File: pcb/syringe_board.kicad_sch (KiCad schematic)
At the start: 33 parts, among them J1 PJ-037A, J2 0855025008, J3 OSTVN08A150, J4 10118194-0001LF, J5 PPTC161LFBN-RC, J6 PPTC121LFBN-RC, U1 TMC2208, U2 ROF-78E3.3-0.5SMD-R, U3 ATMEGA32U4, X1 feather_wing, Y1 8MHz

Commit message: pcb updates in progress
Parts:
- removed J1: PJ-037A, asl_footprints:DC_Jack, symbol asl_symbols:PJ-037A
- removed J4: 10118194-0001LF, asl_footprints:microUSB_horizontal_socket, symbol asl_symbols:USB_micro_horz_socket_reinforced
- removed JP1, JP2: SolderJumper_3_Open, Jumper:SolderJumper-3_P1.3mm_Open_RoundedPad1.0x1.5mm, symbol Jumper:SolderJumper_3_Open
- removed U2: ROF-78E3.3-0.5SMD-R, asl_footprints:DC_DC_CONVERTER, symbol asl_symbols:DC-DC_converter
- removed Y1: 8MHz, Crystal:Resonator_SMD_muRata_CSTxExxV-3Pin_3.0x1.1mm, symbol asl_symbols:Resonator
- added C10: 22µF, Capacitor_SMD:C_1206_3216Metric, symbol Device:C
- added C8: 100nF, Capacitor_SMD:C_0603_1608Metric, symbol Device:C
- added C9: 10µF, Capacitor_SMD:C_1206_3216Metric, symbol Device:C
- added L1: 3.9µH, Inductor_SMD:L_0805_2012Metric, symbol Device:L
- added U2: AP63203WU, Package_TO_SOT_SMD:TSOT-23-6, symbol Regulator_Switching:AP63203WU
- added U4: ATSAMD21E, Package_DFN_QFN:QFN-32-1EP_5x5mm_P0.5mm_EP3.6x3.6mm, symbol asl_symbols_new:ATSAMD21E
- H1, H2, H3, H4: footprint asl_footprints:standoff nut -> asl_footprints:standoff_nut
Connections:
- net RX is gone; now on net DIO_A: U3.20 (PD2(RX)), X1.14 (RX)
- net TX is gone; now on net DIO_B: U3.21 (PD3(TX)), X1.15 (TX)
- new net: U4.10 (GND), U4.28 (GND)

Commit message: PCB v4.0
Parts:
- removed H4: 4207, asl_footprints:standoff_nut, symbol Mechanical:MountingHole
- removed J2: 0855025008, asl_footprints:RJ45_SMD, symbol asl_symbols:RJ45
- removed J3: OSTVN08A150, asl_footprints:8pos_screw_terminal, symbol asl_symbols:Screw_Terminal_01x08
- removed R7: 27Ω, Resistor_SMD:R_0603_1608Metric, symbol Device:R_Small_US
- removed S1: B3FS-1010P, asl_footprints:6mm_tactile_smd, symbol asl_symbols:B3FS-1010P
- removed U2: AP63203WU, Package_TO_SOT_SMD:TSOT-23-6, symbol Regulator_Switching:AP63203WU
- removed U3: ATMEGA32U4, Package_QFP:TQFP-44_10x10mm_P0.8mm, symbol asl_symbols:ATMEGA32U4
- removed U4: ATSAMD21E, Package_DFN_QFN:QFN-32-1EP_5x5mm_P0.5mm_EP3.6x3.6mm, symbol asl_symbols_new:ATSAMD21E
- added C2: 0.1µF, Capacitor_SMD:C_0603_1608Metric, symbol Device:C_Small
- added D1: Red, LED_SMD:LED_0603_1608Metric, symbol Device:LED
- added J1: RJ45_pyControl, asl_footprints:RJ45_SMD, symbol asl_symbols_new:RJ45_pyControl
- added J4: SWD_connector, asl_footprints:SWD_2x5_socket, symbol asl_symbols_new:SWD_connector
- added J5, J8: Conn_01x04_Male, Connector_PinHeader_2.54mm:PinHeader_2x02_P2.54mm_Vertical, symbol Connector:Conn_01x04_Male
- added J6: Male header, Connector_PinHeader_2.54mm:PinHeader_1x07_P2.54mm_Horizontal, symbol Connector:Conn_01x07_Male
- added J7: Female header, Connector_PinSocket_2.54mm:PinSocket_1x07_P2.54mm_Horizontal, symbol Connector:Conn_01x07_Female
- added R1: 10KΩ, Resistor_SMD:R_0603_1608Metric, symbol Device:R_Small_US
- added R2: 1KΩ, Resistor_SMD:R_0603_1608Metric, symbol Device:R_Small_US
- added U1: AP63203WU, Package_TO_SOT_SMD:TSOT-23-6, symbol asl_symbols_new:AP63203WU
- added U2: ATSAMD21G, Package_QFP:TQFP-48_7x7mm_P0.5mm, symbol asl_symbols_new:ATSAMD21G
- H1, H2, H3: value 4207 -> MountingHole; footprint asl_footprints:standoff_nut -> MountingHole:MountingHole_3.2mm_M3
- R6: value 27Ω -> 10KΩ
- U3: renamed from U1; value TMC2208 -> TMC2209
- X1: now left out of the parts list
- renumbered C8 to C1, C6 to C10, C1 to C11, C10 to C3, C9 to C4, C7 to C5, C5 to C6, C2 to C7, C3 to C8, C4 to C9, D1 to D2, J5 to J2, J6 to J3, R4 to R3, R5 to R4, R3 to R5, R2 to R7, R1 to R8
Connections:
- net 3.3VDC is gone; now on net +3V3: C6.2, R3.1, R4.1, U3.15 (VCC_IO), X1.2 (3V)
- net D+ is gone; now on net RST: R6.2
- net LIMIT1 is gone; now on net A3: X1.8 (A3)
- net 12VDC: now also J1.8 (12V)
- net A1: now also U2.7 (PB08(A1))
- net D5: now also U2.24 (PA15(D5))
- net D6: now also U2.29 (PA20(D6)); no longer U3.14 (PDN_UART)
- net D9: now also J6.5 (Pin_5), U2.12 (PA07(D9))
- net GND: now also C3.2, C4.2, C2.2, J1.2 (GND), J4.3 (GND), J4.5 (GND), J4.9 (GNDDetect), J6.7 (Pin_7), R1.2, U1.4 (GND), U2.18 (GND), U2.35 (GND), U2.42 (GND), U2.5 (GNDANA)
- net MISO: now also U2.21 (PA12(MISO))
- net MOSI: now also U2.19 (PB10(MOSI))
- net RST: now also U2.40 (~RESET)
- net SCK: now also U2.20 (PB11(SCK))
- net SCL: now also U2.32 (PA23(SCL))
- net SDA: now also U2.31 (PA22(SDA))
- net at U3.24 (OA1): now also J6.3 (Pin_3)
- net at U3.21 (OA2): now also J6.4 (Pin_4)
- net at U3.26 (OB1): now also J6.2 (Pin_2)
- net at U3.1 (OB2): now also J6.1 (Pin_1)
- net +3V3: now reaches R6.1
- net +3V3: now also C3.1, L1.2, D1.2 (A), J4.1 (VTref), U1.1 (FB), U2.17 (VDDIO), U2.36 (VDDIO), U2.44 (VDDIN), U2.6 (VDDANA)
- net D11: now reaches U3.11 (DIAG)
- net D11: now also X1.23 (D11), U2.25 (PA16(D11))
- net 5VDC: now reaches C4.1
- net 5VDC: now also J1.6 (5V), U1.2 (EN), U1.3 (IN)
- net at C1.1: now also U1.6 (BST)
- net at C1.2: now also L1.1, U1.5 (SW)
- net A renamed A5
- net A5: now also U3.2 (ENN), U2.47 (PB02(A5))
- net AREF: no longer names the net of X1.3 (AREF)
- net AREF: now also U2.4 (PA03(AREF))
- net B renamed A4
- net A4: now also U3.16 (STEP), U2.10 (PA05(A4))
- net CS renamed A2
- net A2: now also U2.8 (PB09(A2))
- net DIO_A renamed RX
- net RX: now also J1.1 (DIO-A), U2.16 (PA11(D0/RX))
- net DIO_B renamed TX
- net TX: now also J1.4 (DIO-B), U2.15 (PA10(D1/TX))
- net DIR renamed A3
- net A3: now also U2.9 (PA04(A3)); no longer X1.22 (D10)
- net IND_LED renamed D13
- net D13: now also U2.26 (PA17(D13))
- net LIMIT2 renamed D12
- net D12: now also U2.28 (PA19(D12))
- net MTR_ENABLE renamed A0
- net A0: now also U2.3 (PA02(A0)); no longer U3.2 (ENN)
- removed net STEP: U3.16 (STEP), X1.23 (D11)
- new net: J7.5 (Pin_5), J8.1 (Pin_1)
- new net: J7.6 (Pin_6), J8.2 (Pin_2)
- new net: J7.7 (Pin_7), J8.3 (Pin_3), J8.4 (Pin_4)
- new net: R2.1, U2.37 (PB22(D30/TX))
- new net: D1.1 (K), R1.1
- new net: J4.2 (SWDIO/TMS), U2.46 (PA31(SWDIO))
- new net: J4.4 (SWDCLK/TCK), U2.45 (PA30(SWCLK))
- new net: C2.1, U2.43 (VDDCORE)
- new net: J5.1 (Pin_1), J7.1 (Pin_1)
- new net: J5.2 (Pin_2), J7.2 (Pin_2)
- new net: J5.3 (Pin_3), J7.3 (Pin_3)
- new net: J5.4 (Pin_4), J7.4 (Pin_4)
- new net D10: J6.6 (Pin_6), U2.27 (PA18(D10)), X1.22 (D10)
- new net PDN_UART: R2.2, U2.38 (PB23(D31/RX)), U3.14 (PDN_UART)
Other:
- moved on the sheet: C1, C10, C11, C3, C4, C5, C6, C7, C8, C9, D2, J2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

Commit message: pcb v4.1
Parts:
- removed J4: SWD_connector, asl_footprints:SWD_2x5_socket, symbol asl_symbols_new:SWD_connector
- added J4: Conn_02x03_Odd_Even, asl_footprints:Tag-Connect_TC2030-IDC-NL_2x03_P1.27mm_Vertical, symbol Connector_Generic:Conn_02x03_Odd_Even
- added U4: AT24C01C-STUM, Package_TO_SOT_SMD:SOT-23-5, symbol asl_symbols_new:AT24C01C-STUM
- C2: value 0.1µF -> 100nF
- C5: value 100uF -> 100µF
- H1, H2, H3: DNP (none) -> 1
- R2: value 1KΩ -> 10KΩ
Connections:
- net +3V3: now also R6.2, J4.1 (Pin_1), U4.4 (Vcc); no longer R6.1
- net GND: now also R2.1, J4.3 (Pin_3), U4.2 (GND), U4.5 (WP)
- net PDN_UART: now also U2.37 (PB22(D30/TX)); no longer U2.38 (PB23(D31/RX))
- net RST: now also R6.1, J4.5 (Pin_5); no longer R6.2
- net SCL: now also U4.1 (SCL)
- net SDA: now also U4.3 (SDA)
- net SWDIO: now reaches U2.46 (PA31(SWDIO))
- net SWDIO: now also J4.2 (Pin_2)
- net SWCLK: now reaches U2.45 (PA30(SWCLK))
- net SWCLK: now also J4.4 (Pin_4)
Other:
- moved on the sheet: R2, R6

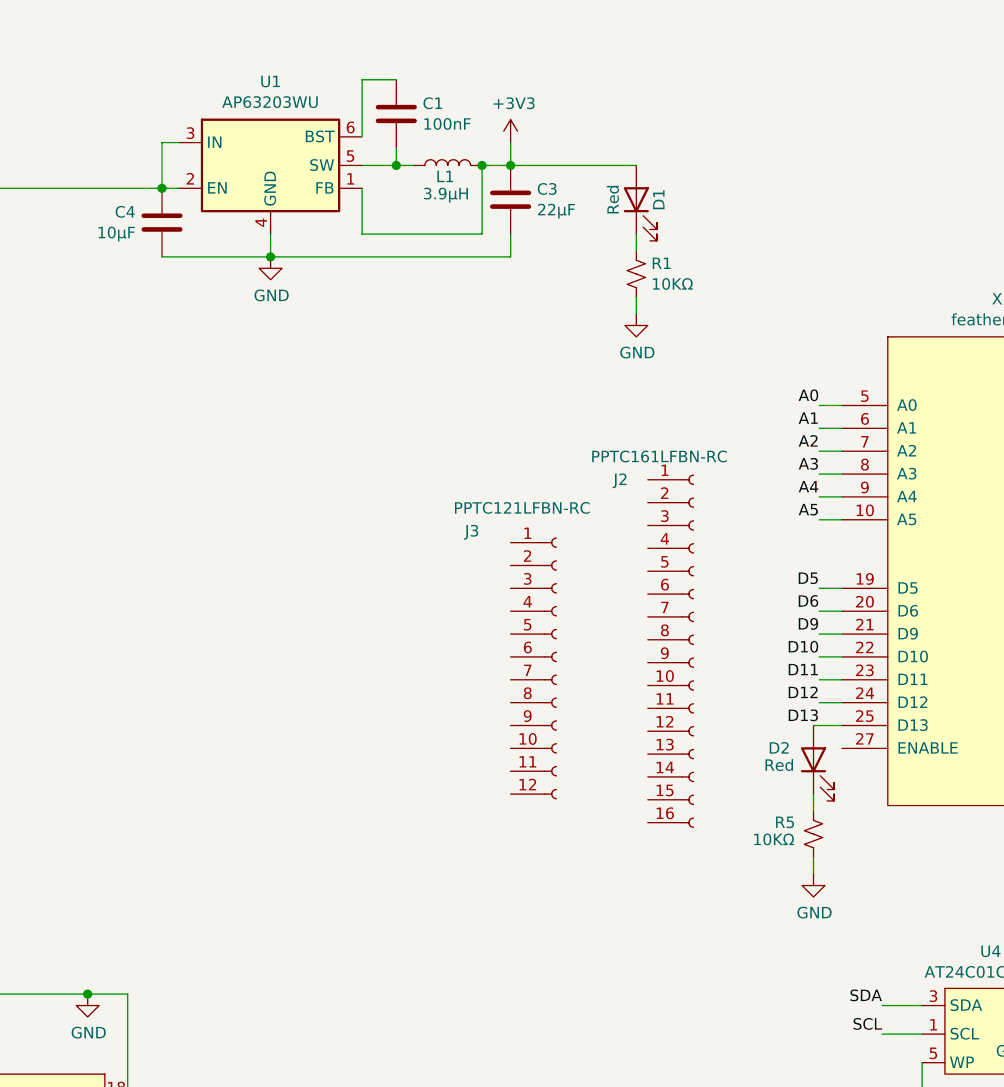
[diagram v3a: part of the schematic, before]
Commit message: PCB v4.2
- changed to different voltage regulator
- shifted feather wing header to avoid collision with RJ45 jack
- removed indicator LEDs
- added pad around m3 mounting hole for improved durability
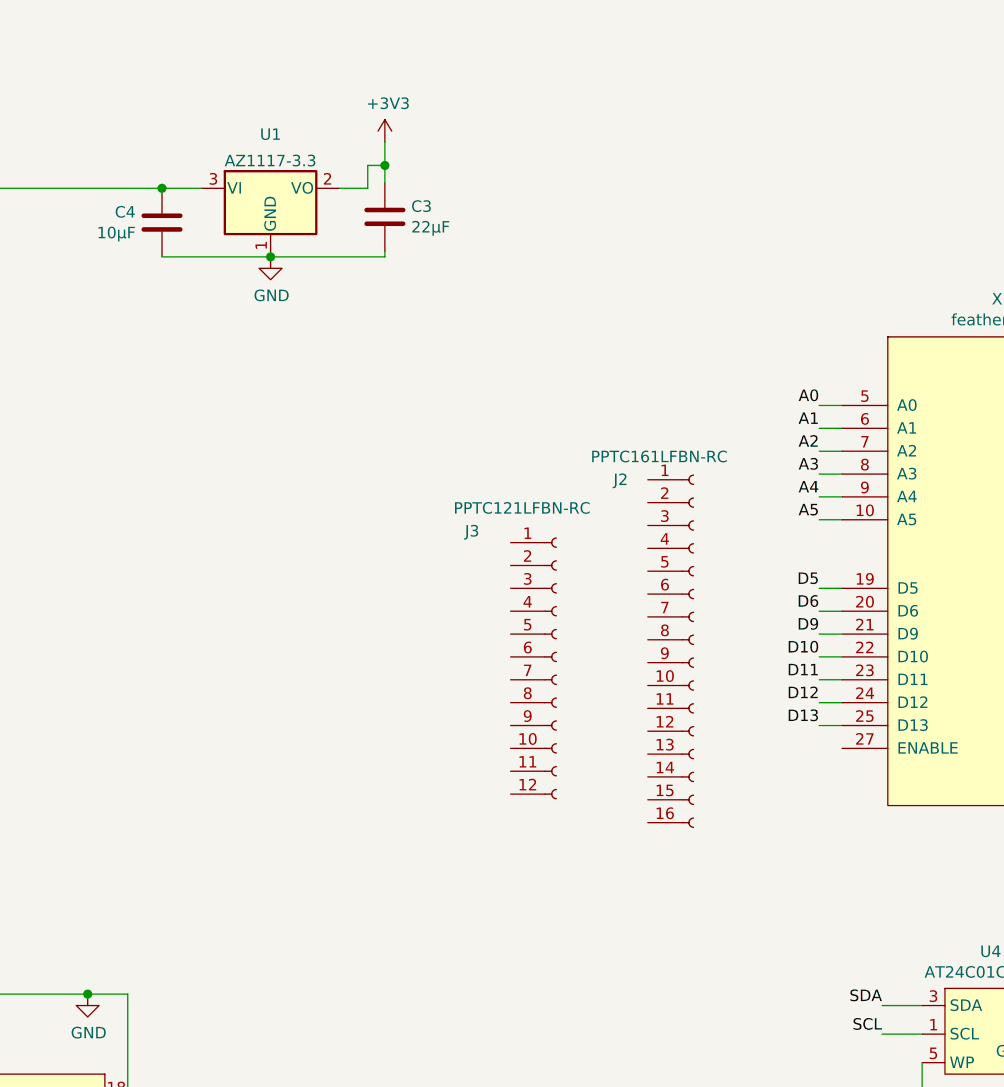
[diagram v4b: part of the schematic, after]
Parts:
- removed C1: 100nF, Capacitor_SMD:C_0603_1608Metric, symbol Device:C
- removed D1, D2: Red, LED_SMD:LED_0603_1608Metric, symbol Device:LED
- removed L1: 3.9µH, Inductor_SMD:L_0805_2012Metric, symbol Device:L
- removed R1, R5: 10KΩ, Resistor_SMD:R_0603_1608Metric, symbol Device:R_Small_US
- removed U1: AP63203WU, Package_TO_SOT_SMD:TSOT-23-6, symbol asl_symbols_new:AP63203WU
- added U1: AZ1117-3.3, Package_TO_SOT_SMD:SOT-223, symbol Regulator_Linear:AZ1117-3.3
- H3: footprint MountingHole:MountingHole_3.2mm_M3 -> MountingHole:MountingHole_3.2mm_M3_DIN965_Pad
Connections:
- net +3V3: now also U1.2 (VO)
- net 5VDC: now also U1.3 (VI)
- net GND: now also U1.1 (GND)
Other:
- title: Syringe Board -> Syringe Control Board
- moved on the sheet: C3
